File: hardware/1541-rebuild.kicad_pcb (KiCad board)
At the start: 2 copper layers, 71.6 x 65.8 mm, 20 parts, among them IC1 ATMEGA1284P-P, IC2 VIA6522, J1 ISP, J2 KEYS, J3 RESET_1541, J4 SD Card Modul Connector, J5 EXT_5V, J6 IO, J7 LCD Display, P1 VIA_PIN_1-20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

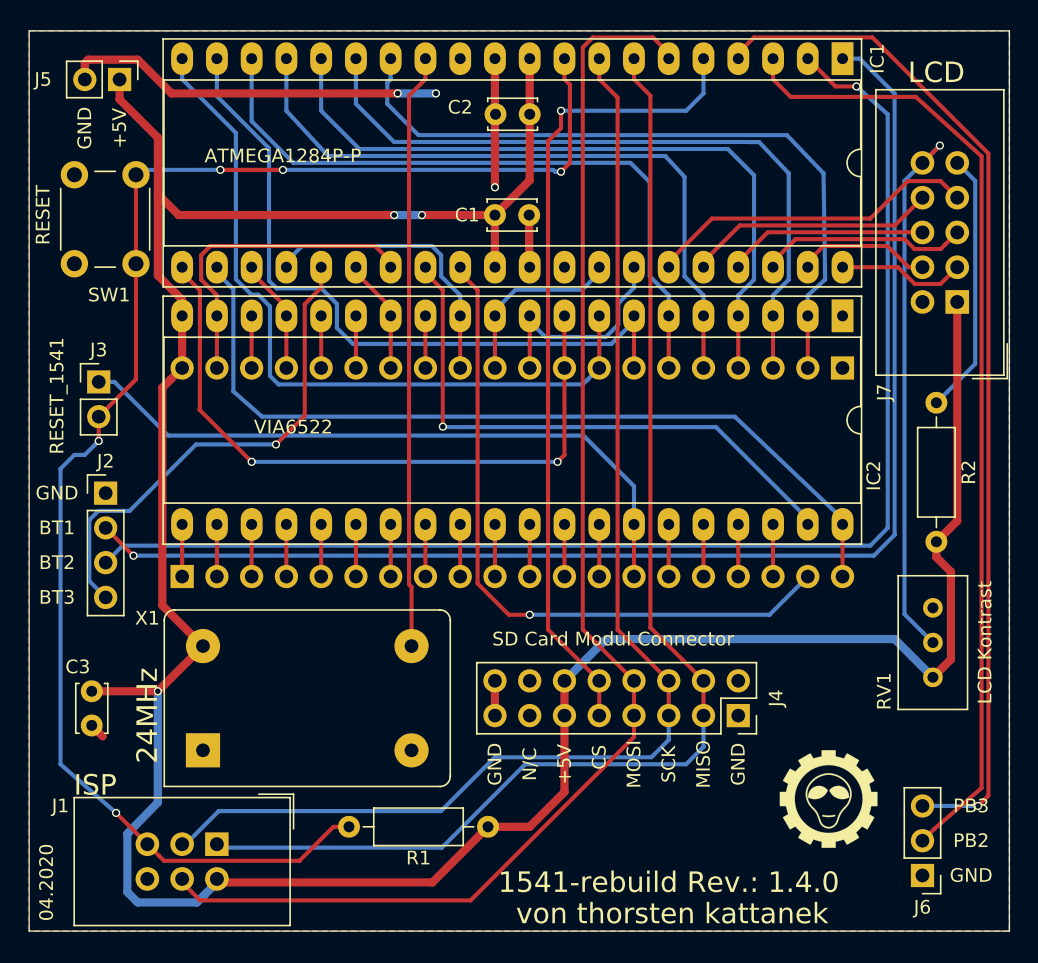
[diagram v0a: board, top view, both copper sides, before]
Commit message: major changes for 1.4.1 PCB
created a new PCB for I2C support. all connections rerouted and
a new board needs to be created. layout and footprint taken from 1.4.0
board revision. images from kicad added, README adopted
CAUTION: PCB untested, due to lack of software routines (I2C)
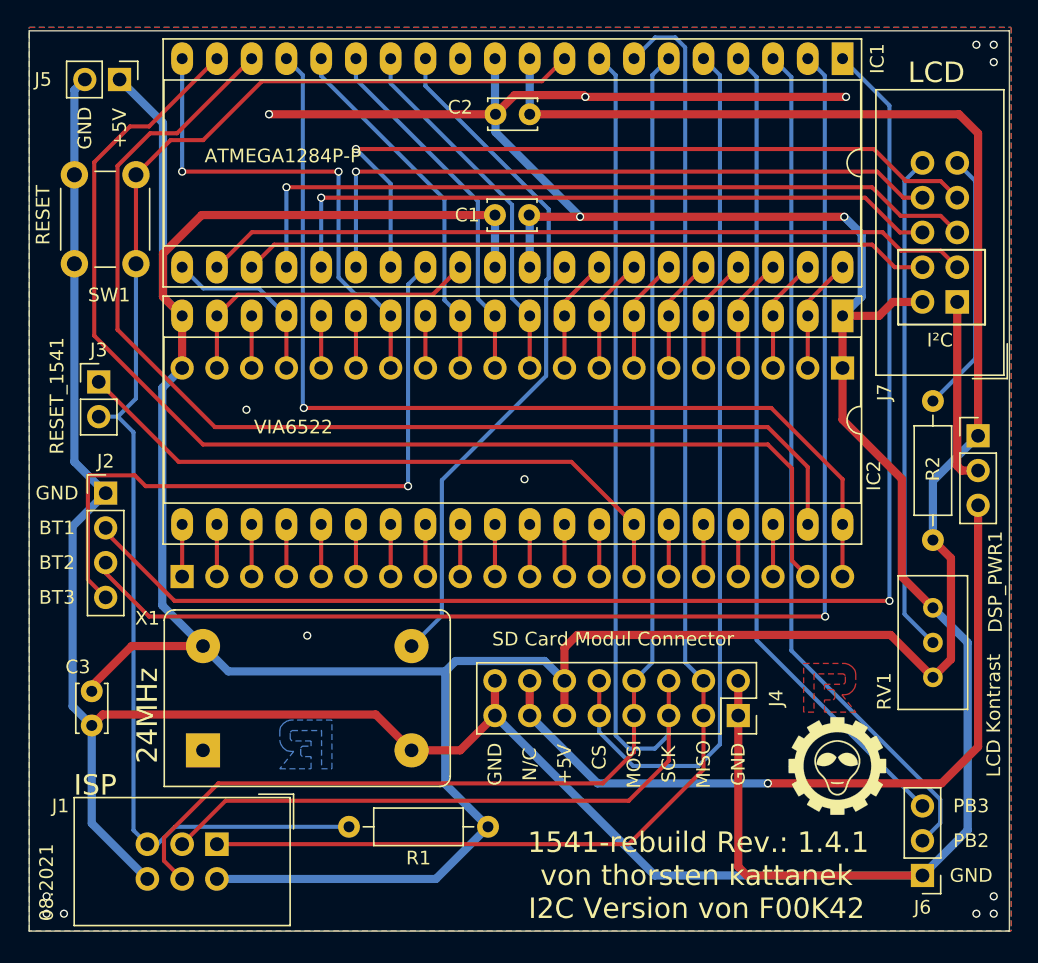
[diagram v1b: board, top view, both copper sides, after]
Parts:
- added DSP_PWR1: IO, Connector_PinHeader_2.54mm:PinHeader_1x03_P2.54mm_Vertical, F.Cu at (177.3, 103.5)
- moved G*** 2.50 mm to (167.0, 127.6)
- moved R2 0.28 mm to (174.0, 101.0)
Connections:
- IC1 pad 14: /VIA 6522 Sockel/PA0 -> /VIA 6522 Sockel/STP1
- IC1 pad 15: /VIA 6522 Sockel/PA1 -> /VIA 6522 Sockel/STP0
- IC1 pad 16: /VIA 6522 Sockel/PA2 -> /VIA 6522 Sockel/MTR
- IC1 pad 17: /VIA 6522 Sockel/PA3 -> /VIA 6522 Sockel/BRDY
- IC1 pad 18: /VIA 6522 Sockel/PA4 -> /VIA 6522 Sockel/SOE
- IC1 pad 19: /VIA 6522 Sockel/PA5 -> /VIA 6522 Sockel/SOE_GA
- IC1 pad 20: /VIA 6522 Sockel/PA6 -> /VIA 6522 Sockel/WPS
- IC1 pad 21: /VIA 6522 Sockel/PA7 -> /VIA 6522 Sockel/SYNC
- IC1 pad 22: /VIA 6522 Sockel/BRDY -> /LCD Display/D4_SCL
- IC1 pad 23: /VIA 6522 Sockel/SYNC -> /LCD Display/D5_SDA
- IC1 pad 24: /VIA 6522 Sockel/MTR -> /LCD Display/D6
- IC1 pad 25: /BT3 -> /LCD Display/D7
- IC1 pad 26: /VIA 6522 Sockel/WPS -> /LCD Display/RS
- IC1 pad 27: /VIA 6522 Sockel/OE -> /LCD Display/EN
- IC1 pad 28: /VIA 6522 Sockel/SOE -> /BT3
- IC1 pad 29: /VIA 6522 Sockel/SOE_GA -> /VIA 6522 Sockel/OE
- IC1 pad 33: /VIA 6522 Sockel/SPT0 -> /VIA 6522 Sockel/PA7
- IC1 pad 34: /VIA 6522 Sockel/STP1 -> /VIA 6522 Sockel/PA6
- IC1 pad 35: /LCD Display/EN -> /VIA 6522 Sockel/PA5
- IC1 pad 36: /LCD Display/RS -> /VIA 6522 Sockel/PA4
- IC1 pad 37: /LCD Display/D7 -> /VIA 6522 Sockel/PA3
- IC1 pad 38: /LCD Display/D6 -> /VIA 6522 Sockel/PA2
- IC1 pad 39: /LCD Display/D5 -> /VIA 6522 Sockel/PA1
- IC1 pad 40: /LCD Display/D4 -> /VIA 6522 Sockel/PA0
- IC2 pad 11: /VIA 6522 Sockel/SPT0 -> /VIA 6522 Sockel/STP0
- J4 pad 13: Net-(J4-Pad13) -> +3V3
- J4 pad 14: Net-(J4-Pad14) -> +3V3
- J7 pad 1: +5V -> /LCD Display/DSP_PWR
- J7 pad 3: /LCD Display/D4 -> /LCD Display/D4_SCL
- J7 pad 4: /LCD Display/D5 -> /LCD Display/D5_SDA
- P1 pad 11: /VIA 6522 Sockel/SPT0 -> /VIA 6522 Sockel/STP0
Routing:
- net GND: track 44.9 -> 305.3 mm, vias 3 -> 17
- net /LCD Display/D4_SCL: track 0.00 -> 56.2 mm
- net +3V3: track 0.00 -> 56.1 mm, vias 0 -> 1
- net +5V: track 213.9 -> 264.5 mm, vias 3 -> 0
- net /LCD Display/D5_SDA: track 0.00 -> 50.4 mm
- net /VIA 6522 Sockel/PA6: track 54.8 -> 8.42 mm
- net /VIA 6522 Sockel/PA5: track 52.3 -> 8.42 mm
- net /VIA 6522 Sockel/PA0: track 52.2 -> 8.42 mm
- net /VIA 6522 Sockel/PA2: track 52.0 -> 8.42 mm
- net /VIA 6522 Sockel/PA1: track 51.8 -> 8.42 mm
- net /VIA 6522 Sockel/SOE: track 42.0 -> 83.8 mm, vias 1 -> 0
- net /VIA 6522 Sockel/PA4: track 49.7 -> 8.42 mm
- net /VIA 6522 Sockel/PA7: track 49.6 -> 8.42 mm, vias 2 -> 0
- net /VIA 6522 Sockel/PA3: track 49.6 -> 8.42 mm
- net /LCD Display/D6: track 15.3 -> 56.2 mm, vias 0 -> 1
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- added copper zone on B.Cu, net (none)
- added copper zone on F.Cu, net (none)
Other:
- board text added: "08.2021"
- board text added: "1541-rebuild Rev.: 1.4.1"
- board text added: "I2C Version von F00K42"
- board text added: "I²C"
- board text added: "https://github.com/fook42/1541-rebuild"
- board text removed: "04.2020"
- board text removed: "1541-rebuild Rev.: 1.4.0"
- board text removed: "https://github.com/ThKattanek/1541-rebuild"

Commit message: modified 1.4.1 PCB
added capacitor for better power-supply stability
minor changes for silkscreen texts and groundplane
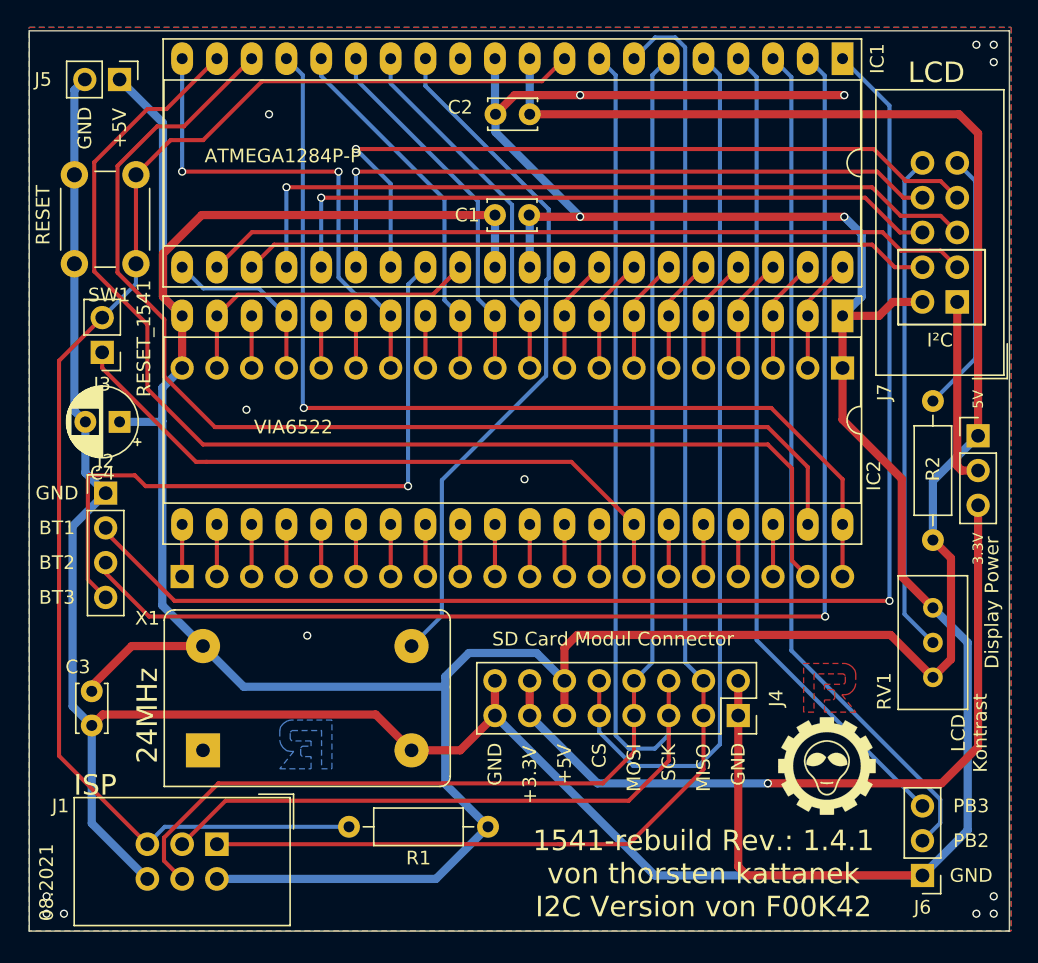
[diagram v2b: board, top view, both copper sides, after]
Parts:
- added C4: 47µF, Capacitor_THT:CP_Radial_D5.0mm_P2.50mm, F.Cu at (114.6, 102.5)
- Display Power: renamed from DSP_PWR1
- moved J3 2.17 mm to (113.3, 97.4), turned to 180 degrees
- moved G*** 0.76 mm to (166.2, 127.6)
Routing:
- net GND: track 305.3 -> 288.6 mm
- net +5V: track 264.5 -> 268.4 mm
- net Net-(IC1-Pad9): track 101.8 -> 104.0 mm
- net /VIA 6522 Sockel/~RESET: track 47.2 -> 48.6 mm
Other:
- board text added: "+3.3V"
- board text added: "1541-rebuild Rev.: 1.4.1 von thorsten kattanek I2C Version von F00K42"
- board text added: "3.3V"
- board text added: "5V"
- board text removed: "1541-rebuild Rev.: 1.4.1"
- board text removed: "I2C Version von F00K42"
- board text removed: "N/C"
- board text removed: "von thorsten kattanek"

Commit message: PCB revision 1.4.2
included capacitor for stabilization
better ground-plane design (more coverage)
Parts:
- Display_Power1: renamed from Display Power; value IO -> Display Power
- J4: value SD Card Modul Connector -> SD Card Module Connector
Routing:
- net MOSI: track 92.2 -> 105.0 mm
- net SCK: track 100.0 -> 91.5 mm
- net CS: track 64.8 -> 68.9 mm
- net MISO: track 97.0 -> 93.0 mm
- net GND: track 288.6 -> 291.7 mm
- net /LCD Display/EN: track 55.1 -> 52.6 mm
- net PB2: track 62.8 -> 64.6 mm
- net +5V: track 268.4 -> 267.5 mm
- net +3V3: track 56.1 -> 56.9 mm
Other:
- board text added: "1541-rebuild Rev.: 1.4.2 von thorsten kattanek I2C Version von F00K42"
- board text added: "LCD Contrast"
- board text removed: "1541-rebuild Rev.: 1.4.1 von thorsten kattanek I2C Version von F00K42"
- board text removed: "LCD Kontrast"
